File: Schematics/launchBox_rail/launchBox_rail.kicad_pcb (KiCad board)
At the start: 2 copper layers, 40.8 x 52.1 mm, 18 parts, among them J1 Screw_Terminal_01x02, J2 Conn_01x04_Pin, J3 Screw_Terminal_01x02, Q1 NMOS, SW1 SW_MEC_5G

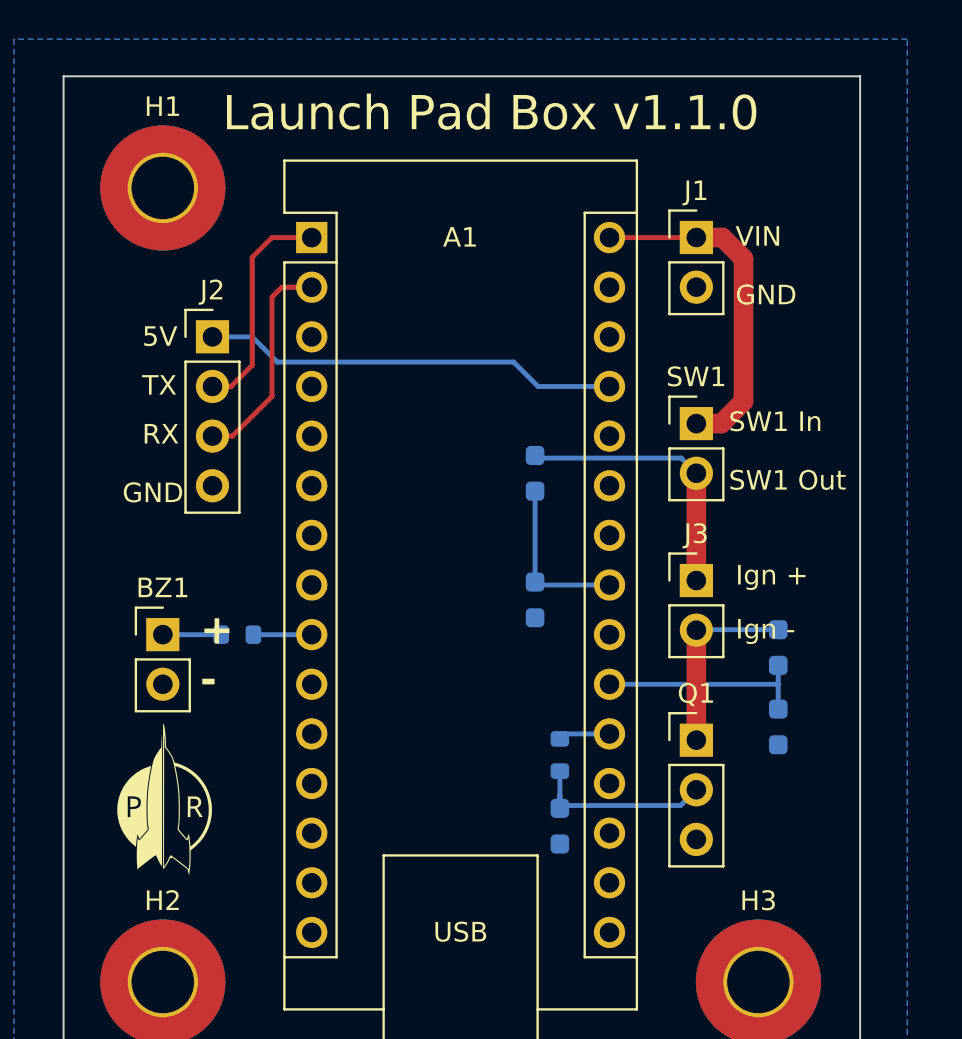
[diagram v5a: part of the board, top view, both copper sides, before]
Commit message: Removed some of the of the component designators from the silkscreen
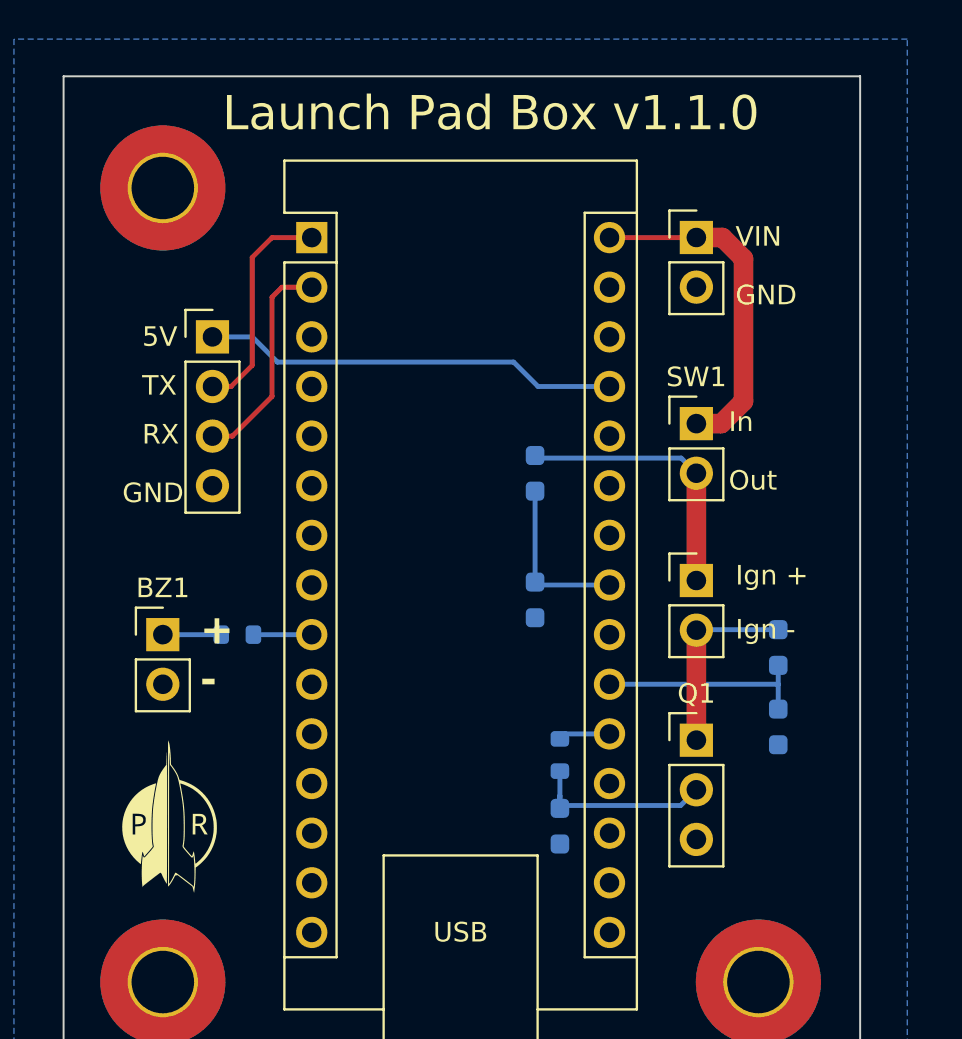
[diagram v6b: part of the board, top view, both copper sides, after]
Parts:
- moved G*** 0.92 mm to (91.7, 82.8)
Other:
- board text added: "In"
- board text added: "Out"
- board text removed: "SW1 In"
- board text removed: "SW1 Out"
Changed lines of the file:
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@@
 			(at 0 -2.38 0)
 			(layer "F.SilkS")
+			(hide yes)
 			(effects
 				(font
@@
 	(footprint "logo:Logo"
 		(layer "F.Cu")
-		(at 91.44 81.915)
+		(at 91.694 82.804)
 		(property "Reference" "G***"
 			(at 0 0 0)
@@
 			(at 0 -2.38 0)
 			(layer "F.SilkS")
+			(hide yes)
 			(effects
 				(font
@@
 			(at 0 -4.15 0)
 			(layer "F.SilkS")
+			(hide yes)
 			(effects
 				(font
@@
 			(at 0 -4.15 0)
 			(layer "F.SilkS")
+			(hide yes)
 			(effects
 				(font
@@
 			(at 0 -4.15 0)
 			(layer "F.SilkS")
+			(hide yes)
 			(effects
 				(font
@@
 			(at 7.62 0 0)
 			(layer "F.SilkS")
+			(hide yes)
 			(effects
 				(font
@@
 			(at 0 -2.38 0)
 			(layer "F.SilkS")
+			(hide yes)
 			(effects
 				(font
@@
 		)
 	)
-	(gr_text "SW1 Out"
+	(gr_text "Out"
 		(at 120.396 66.36 0)
 		(layer "F.SilkS")
@@
 		)
 	)
-	(gr_text "SW1 In"
+	(gr_text "In"
 		(at 120.396 63.36 0)
 		(layer "F.SilkS")
@@
 	)
 	(group ""
-		(members "0e9a45ad-2ccd-4c20-82d6-20de529e2370" "17d5c1b7-8eab-48d1-8feb-89a5fd7ca4e3"
-			"46843de9-f1ae-4b66-881b-c162d3ac92af" "948eea1b-df2a-4b29-b598-63c67604af17"
-			"f54e5c48-b5fc-4634-9ab8-971e7da5928b"
+		(members "0a5d2dc9-061d-43d7-a648-1f5bb1d03fff" "7a3ea3e2-8d97-4630-b69b-6c049bb16100"
+			"b97a5974-38fb-4299-a725-e20eba3cf6de"
 		)
 	)
@@
 	)
 	(group ""
-		(members "0a5d2dc9-061d-43d7-a648-1f5bb1d03fff" "7a3ea3e2-8d97-4630-b69b-6c049bb16100"
-			"b97a5974-38fb-4299-a725-e20eba3cf6de"
+		(members "0e9a45ad-2ccd-4c20-82d6-20de529e2370" "17d5c1b7-8eab-48d1-8feb-89a5fd7ca4e3"
+			"46843de9-f1ae-4b66-881b-c162d3ac92af" "948eea1b-df2a-4b29-b598-63c67604af17"
+			"f54e5c48-b5fc-4634-9ab8-971e7da5928b"
 		)
 	)
 	(group ""
 		(members "0be55ec3-0673-4b91-bc9b-4347a262f02b" "638f19fc-76b9-4aa4-b3d8-243c415282aa"
-			"a7122983-a21e-491b-91d0-4d3b9f6ac649" "d8d969a3-31ee-4c61-a8ea-76a7f2eb4491"
-			"e6e49a03-15cf-40ca-8a4e-a4b36c0d7501"
+			"a7122983-a21e-491b-91d0-4d3b9f6ac649"
 		)
 	)
